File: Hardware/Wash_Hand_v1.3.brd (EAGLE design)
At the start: 71.1 x 48.3 mm, 62 parts, among them IC1 LM358D, IC2 LP298XS, IC3 405016TSSOP, J1 I2C, J2 ICSP, J3 SPI, J4 9V_CONN, J5 EXT_VCC, J6 6_PIN_SERIAL_CABLEPTH, Q1 16.0 Mhz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

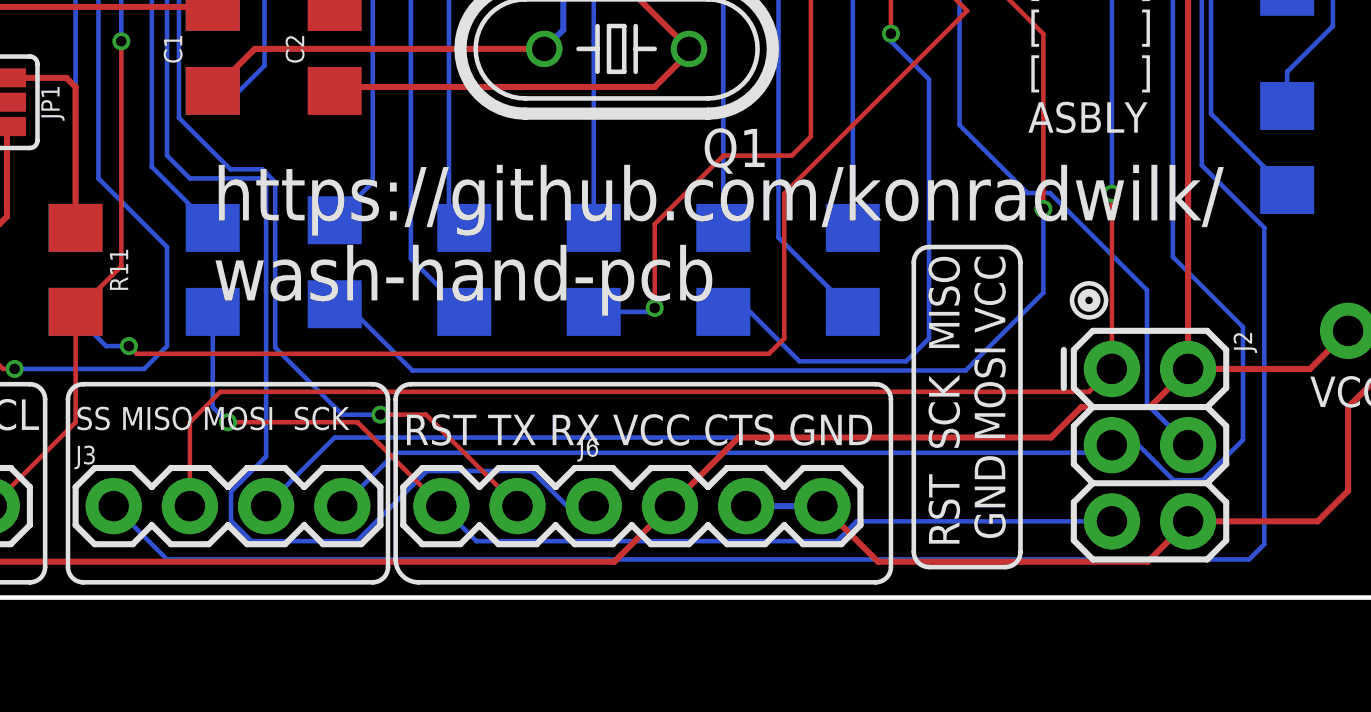
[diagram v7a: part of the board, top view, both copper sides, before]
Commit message: Board/Schematic: Use RESET instead of DTR on ICSP
We don't want the line past the 0.1uF cap to go
in the ICSP but instead use the one that goes directly
to the RESET pin.

Signed-off-by: Konrad Rzeszutek Wilk <konrad@kernel.org>
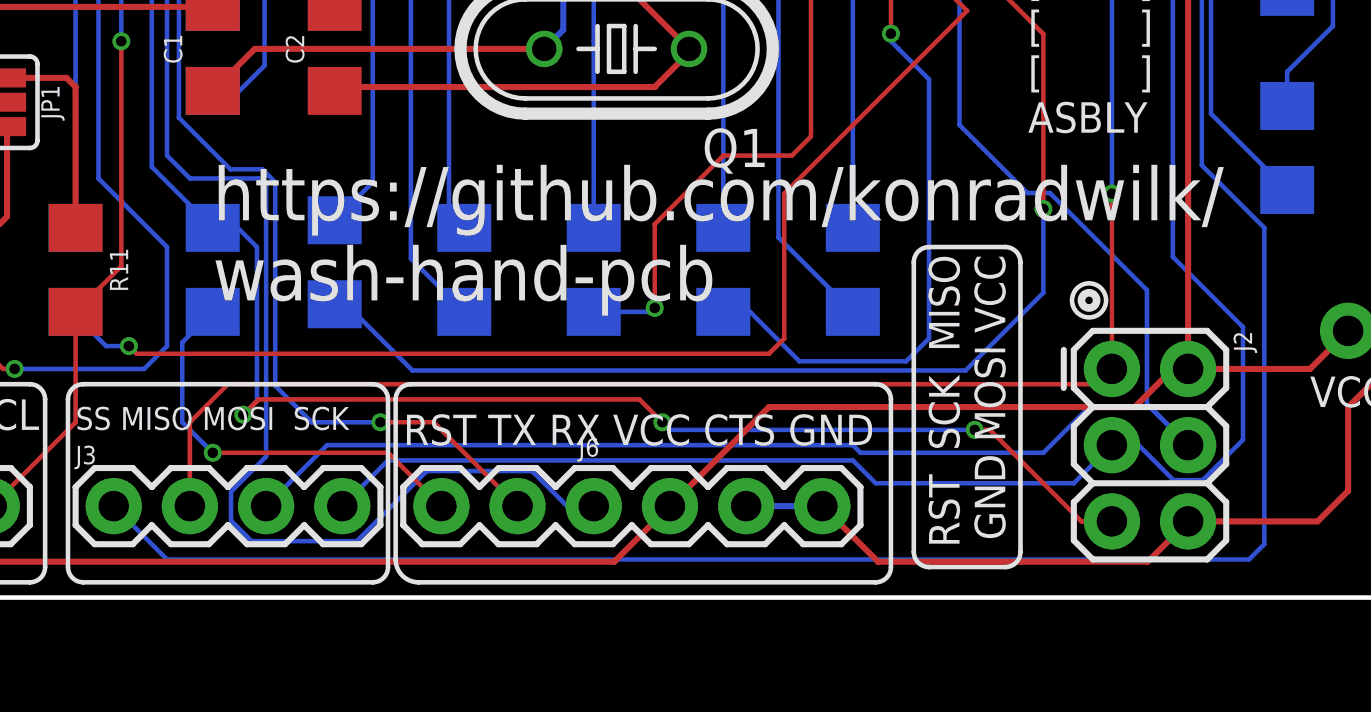
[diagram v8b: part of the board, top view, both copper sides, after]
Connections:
- net DTR: no longer J2.5
- net RESET: now also J2.5
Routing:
- net RESET: track 42.5 -> 80.8 mm, vias 1 -> 4
- net DTR: track 35.3 -> 13.9 mm
- net TX: track 36.2 -> 36.9 mm
- net SCK: track 107.7 -> 108.3 mm
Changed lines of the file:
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@@
 <wire x1="34.16" y1="43.05" x2="32.258" y2="41.148" width="0.1524" layer="1"/>
 <wire x1="30.734" y1="35.306" x2="32.004" y2="34.036" width="0.1524" layer="1"/>
+<contactref element="J2" pad="5"/>
+<wire x1="25.654" y1="12.322" x2="26.4892" y2="12.322" width="0.1524" layer="16"/>
+<wire x1="26.4892" y1="12.322" x2="27.1272" y2="11.684" width="0.1524" layer="16"/>
+<wire x1="27.1272" y1="11.684" x2="27.1272" y2="6.5532" width="0.1524" layer="16"/>
+<wire x1="55.626" y1="2.54" x2="54.61" y2="2.54" width="0.1524" layer="1"/>
+<wire x1="54.61" y1="2.54" x2="51.562" y2="5.588" width="0.1524" layer="1"/>
+<wire x1="51.562" y1="5.588" x2="51.054" y2="5.588" width="0.1524" layer="1"/>
+<wire x1="27.1272" y1="6.5532" x2="26.67" y2="6.096" width="0.1524" layer="16"/>
+<via x="26.67" y="6.096" extent="1-16" drill="0.35"/>
+<wire x1="26.67" y1="6.096" x2="27.178" y2="6.604" width="0.1524" layer="1"/>
+<wire x1="27.178" y1="6.604" x2="39.878" y2="6.604" width="0.1524" layer="1"/>
+<wire x1="39.878" y1="6.604" x2="40.64" y2="5.842" width="0.1524" layer="1"/>
+<via x="40.64" y="5.842" extent="1-16" drill="0.35"/>
+<wire x1="51.054" y1="5.588" x2="40.894" y2="5.588" width="0.1524" layer="16"/>
+<wire x1="40.894" y1="5.588" x2="40.64" y2="5.842" width="0.1524" layer="16"/>
+<via x="51.054" y="5.588" extent="1-16" drill="0.35"/>
 </signal>
 <signal name="VCC">
@@
 <wire x1="39.0398" y1="1.1938" x2="40.894" y2="3.048" width="0.2032" layer="1"/>
 <wire x1="13.0302" y1="1.1938" x2="39.0398" y2="1.1938" width="0.2032" layer="1"/>
-<wire x1="58.166" y1="7.62" x2="56.896" y2="6.35" width="0.2032" layer="1"/>
-<wire x1="56.896" y1="6.35" x2="54.61" y2="6.35" width="0.2032" layer="1"/>
-<wire x1="54.61" y1="6.35" x2="53.594" y2="5.334" width="0.2032" layer="1"/>
-<wire x1="43.18" y1="5.334" x2="40.894" y2="3.048" width="0.2032" layer="1"/>
-<wire x1="53.594" y1="5.334" x2="43.18" y2="5.334" width="0.2032" layer="1"/>
+<wire x1="58.166" y1="7.62" x2="57.658" y2="7.62" width="0.2032" layer="1"/>
+<wire x1="57.658" y1="7.62" x2="56.388" y2="6.35" width="0.2032" layer="1"/>
+<wire x1="44.196" y1="6.35" x2="40.894" y2="3.048" width="0.2032" layer="1"/>
+<wire x1="56.388" y1="6.35" x2="44.196" y2="6.35" width="0.2032" layer="1"/>
 <wire x1="18.796" y1="16.51" x2="17.018" y2="16.51" width="0.2032" layer="1"/>
 <wire x1="17.018" y1="16.51" x2="10.16" y2="9.652" width="0.2032" layer="1"/>
@@
 <contactref element="J3" pad="3"/>
 <contactref element="IC3" pad="5"/>
-<wire x1="27.432" y1="3.048" x2="29.718" y2="5.334" width="0.1524" layer="16"/>
-<wire x1="53.594" y1="5.334" x2="54.61" y2="6.35" width="0.1524" layer="16"/>
-<wire x1="54.61" y1="6.35" x2="56.896" y2="6.35" width="0.1524" layer="16"/>
+<wire x1="29.464" y1="5.08" x2="27.432" y2="3.048" width="0.1524" layer="16"/>
+<wire x1="56.896" y1="6.35" x2="54.864" y2="6.35" width="0.1524" layer="16"/>
 <wire x1="56.896" y1="6.35" x2="58.166" y2="5.08" width="0.1524" layer="16"/>
-<wire x1="29.718" y1="5.334" x2="53.594" y2="5.334" width="0.1524" layer="16"/>
 <via x="19.812" y="38.608" extent="1-16" drill="0.35"/>
 <contactref element="U2" pad="15"/>
@@
 <wire x1="12.263" y1="40.457" x2="12.263" y2="39.7542" width="0.1524" layer="1"/>
 <wire x1="17.526" y1="40.894" x2="12.7" y2="40.894" width="0.1524" layer="1"/>
+<wire x1="47.244" y1="4.826" x2="46.99" y2="5.08" width="0.1524" layer="16"/>
+<wire x1="46.99" y1="5.08" x2="29.464" y2="5.08" width="0.1524" layer="16"/>
+<wire x1="54.864" y1="6.35" x2="53.34" y2="4.826" width="0.1524" layer="16"/>
+<wire x1="53.34" y1="4.826" x2="47.244" y2="4.826" width="0.1524" layer="16"/>
 </signal>
 <signal name="D1">
@@
 <via x="9.144" y="37.592" extent="1-16" drill="0.35"/>
 <wire x1="9.144" y1="37.592" x2="26.67" y2="37.592" width="0.1524" layer="16"/>
-<wire x1="55.626" y1="7.62" x2="54.864" y2="6.858" width="0.1524" layer="1"/>
-<wire x1="54.864" y1="6.858" x2="25.908" y2="6.858" width="0.1524" layer="1"/>
-<wire x1="25.908" y1="6.858" x2="24.892" y2="5.842" width="0.1524" layer="1"/>
+<wire x1="55.626" y1="7.62" x2="55.118" y2="7.112" width="0.1524" layer="1"/>
+<wire x1="55.118" y1="7.112" x2="26.162" y2="7.112" width="0.1524" layer="1"/>
+<wire x1="26.162" y1="7.112" x2="24.892" y2="5.842" width="0.1524" layer="1"/>
 <wire x1="24.892" y1="5.842" x2="24.892" y2="3.048" width="0.1524" layer="1"/>
 <via x="26.67" y="37.592" extent="1-16" drill="0.35"/>
@@
 <contactref element="J3" pad="4"/>
 <contactref element="IC3" pad="7"/>
-<wire x1="55.626" y1="5.08" x2="55.372" y2="4.826" width="0.1524" layer="16"/>
-<wire x1="31.75" y1="4.826" x2="29.972" y2="3.048" width="0.1524" layer="16"/>
-<wire x1="55.372" y1="4.826" x2="31.75" y2="4.826" width="0.1524" layer="16"/>
+<wire x1="31.496" y1="4.572" x2="29.972" y2="3.048" width="0.1524" layer="16"/>
 <wire x1="57.68203125" y1="3.9116" x2="58.64996875" y2="3.9116" width="0.1524" layer="16"/>
 <wire x1="59.9948" y1="9.01625625" x2="57.658" y2="11.35305625" width="0.1524" layer="16"/>
@@
 <wire x1="14.986" y1="36.83" x2="13.563" y2="38.253" width="0.1524" layer="1"/>
 <wire x1="13.563" y1="38.253" x2="13.563" y2="39.7542" width="0.1524" layer="1"/>
+<wire x1="55.626" y1="5.08" x2="54.356" y2="3.81" width="0.1524" layer="16"/>
+<wire x1="47.752" y1="3.81" x2="46.99" y2="4.572" width="0.1524" layer="16"/>
+<wire x1="46.99" y1="4.572" x2="31.496" y2="4.572" width="0.1524" layer="16"/>
+<wire x1="54.356" y1="3.81" x2="47.752" y2="3.81" width="0.1524" layer="16"/>
 </signal>
 <signal name="D4">
@@
 <signal name="DTR">
 <contactref element="C3" pad="1"/>
-<contactref element="J2" pad="5"/>
 <contactref element="J6" pad="DTR"/>
-<wire x1="55.626" y1="2.54" x2="47.11836875" y2="2.54" width="0.1524" layer="16"/>
-<wire x1="47.11836875" y1="2.54" x2="46.45796875" y2="1.8796" width="0.1524" layer="16"/>
-<wire x1="46.45796875" y1="1.8796" x2="34.4424" y2="1.8796" width="0.1524" layer="16"/>
-<wire x1="34.4424" y1="1.8796" x2="33.274" y2="3.048" width="0.1524" layer="16"/>
-<wire x1="33.274" y1="3.048" x2="30.48" y2="5.842" width="0.1524" layer="1"/>
-<wire x1="30.48" y1="5.842" x2="26.162" y2="5.842" width="0.1524" layer="1"/>
-<via x="26.162" y="5.842" extent="1-16" drill="0.35"/>
-<wire x1="26.162" y1="5.842" x2="25.654" y2="6.35" width="0.1524" layer="16"/>
-<wire x1="25.654" y1="6.35" x2="25.654" y2="9.522" width="0.1524" layer="16"/>
+<wire x1="33.274" y1="3.048" x2="31.496" y2="4.826" width="0.1524" layer="1"/>
+<wire x1="31.496" y1="4.826" x2="25.654" y2="4.826" width="0.1524" layer="1"/>
+<via x="25.654" y="4.826" extent="1-16" drill="0.35"/>
+<wire x1="25.654" y1="4.826" x2="24.638" y2="5.842" width="0.1524" layer="16"/>
+<wire x1="24.638" y1="8.506" x2="24.638" y2="5.842" width="0.1524" layer="16"/>
+<wire x1="24.638" y1="8.506" x2="25.654" y2="9.522" width="0.1524" layer="16"/>
 </signal>
 <signal name="TX">
 <contactref element="J6" pad="RXI"/>
-<wire x1="27.7368" y1="8.3312" x2="29.972" y2="6.096" width="0.1524" layer="16"/>
+<wire x1="27.7368" y1="7.0612" x2="28.956" y2="5.842" width="0.1524" layer="16"/>
 <wire x1="27.30425625" y1="14.2748" x2="27.7368" y2="13.84225625" width="0.1524" layer="16"/>
-<wire x1="27.7368" y1="13.84225625" x2="27.7368" y2="8.3312" width="0.1524" layer="16"/>
+<wire x1="27.7368" y1="13.84225625" x2="27.7368" y2="7.0612" width="0.1524" layer="16"/>
 <wire x1="26.2439125" y1="14.2748" x2="27.30425625" y2="14.2748" width="0.1524" layer="16"/>
 <wire x1="24.5254" y1="15.9933125" x2="26.2439125" y2="14.2748" width="0.1524" layer="16"/>
 <wire x1="24.5254" y1="24.5254" x2="24.5254" y2="15.9933125" width="0.1524" layer="16"/>
-<wire x1="29.972" y1="6.096" x2="31.242" y2="6.096" width="0.1524" layer="16"/>
-<via x="31.242" y="6.096" extent="1-16" drill="0.35"/>
-<wire x1="35.814" y1="3.048" x2="32.766" y2="6.096" width="0.1524" layer="1"/>
-<wire x1="32.766" y1="6.096" x2="31.242" y2="6.096" width="0.1524" layer="1"/>
+<wire x1="31.242" y1="5.842" x2="28.956" y2="5.842" width="0.1524" layer="16"/>
+<via x="31.242" y="5.842" extent="1-16" drill="0.35"/>
+<wire x1="35.814" y1="3.048" x2="33.02" y2="5.842" width="0.1524" layer="1"/>
+<wire x1="33.02" y1="5.842" x2="31.242" y2="5.842" width="0.1524" layer="1"/>
 <contactref element="U2" pad="31"/>
 <wire x1="24.5254" y1="24.5254" x2="28.194" y2="28.194" width="0.1524" layer="16"/>
